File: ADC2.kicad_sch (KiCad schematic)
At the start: 28 parts, among them U107 ADR4540, U111 ADA4841-1

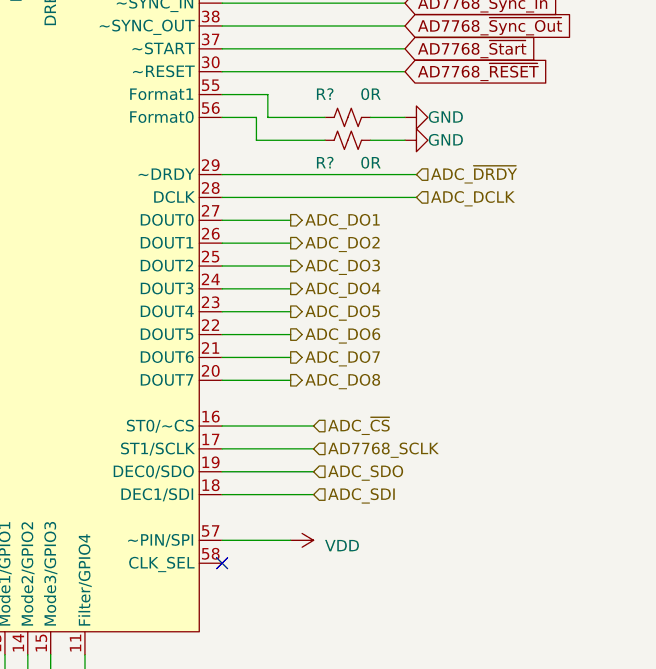
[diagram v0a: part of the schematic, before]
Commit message: Updated Schmatics
Some outdated schematics were in the init commit. Uploded proper revision with tweaks.
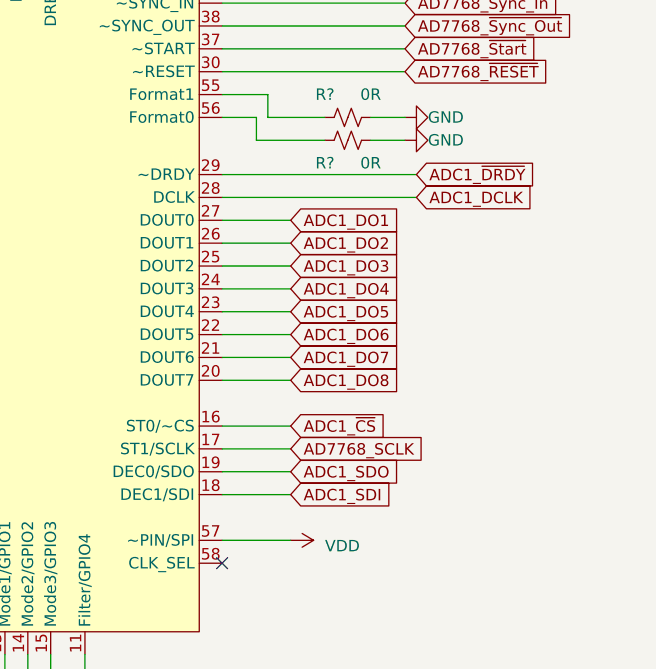
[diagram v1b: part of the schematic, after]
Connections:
- net ADC_DCLK renamed ADC1_DCLK
- net ADC_DO1 renamed ADC1_DO1
- net ADC_DO2 renamed ADC1_DO2
- net ADC_DO3 renamed ADC1_DO3
- net ADC_DO4 renamed ADC1_DO4
- net ADC_DO5 renamed ADC1_DO5
- net ADC_DO6 renamed ADC1_DO6
- net ADC_DO7 renamed ADC1_DO7
- net ADC_DO8 renamed ADC1_DO8
- net ADC_SDI renamed ADC1_SDI
- net ADC_SDO renamed ADC1_SDO
- net ADC_~{CS} renamed ADC1_~{CS}
- net ADC_~{DRDY} renamed ADC1_~{DRDY}
